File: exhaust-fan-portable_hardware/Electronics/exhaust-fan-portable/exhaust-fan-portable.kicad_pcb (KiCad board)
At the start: 2 copper layers, 68 parts, among them J1 Conn_01x04_Pin, J2 Conn_01x04_Pin, J3 Conn_01x04_Pin, J4 Conn_01x04_Pin, J6 Barrel_Jack_MountingPin, J7 Conn_01x04_Pin, J9 Conn_01x06_Socket, P1 USB_C_Plug_USB2.0, Q1 NMOS, Q2 NMOS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

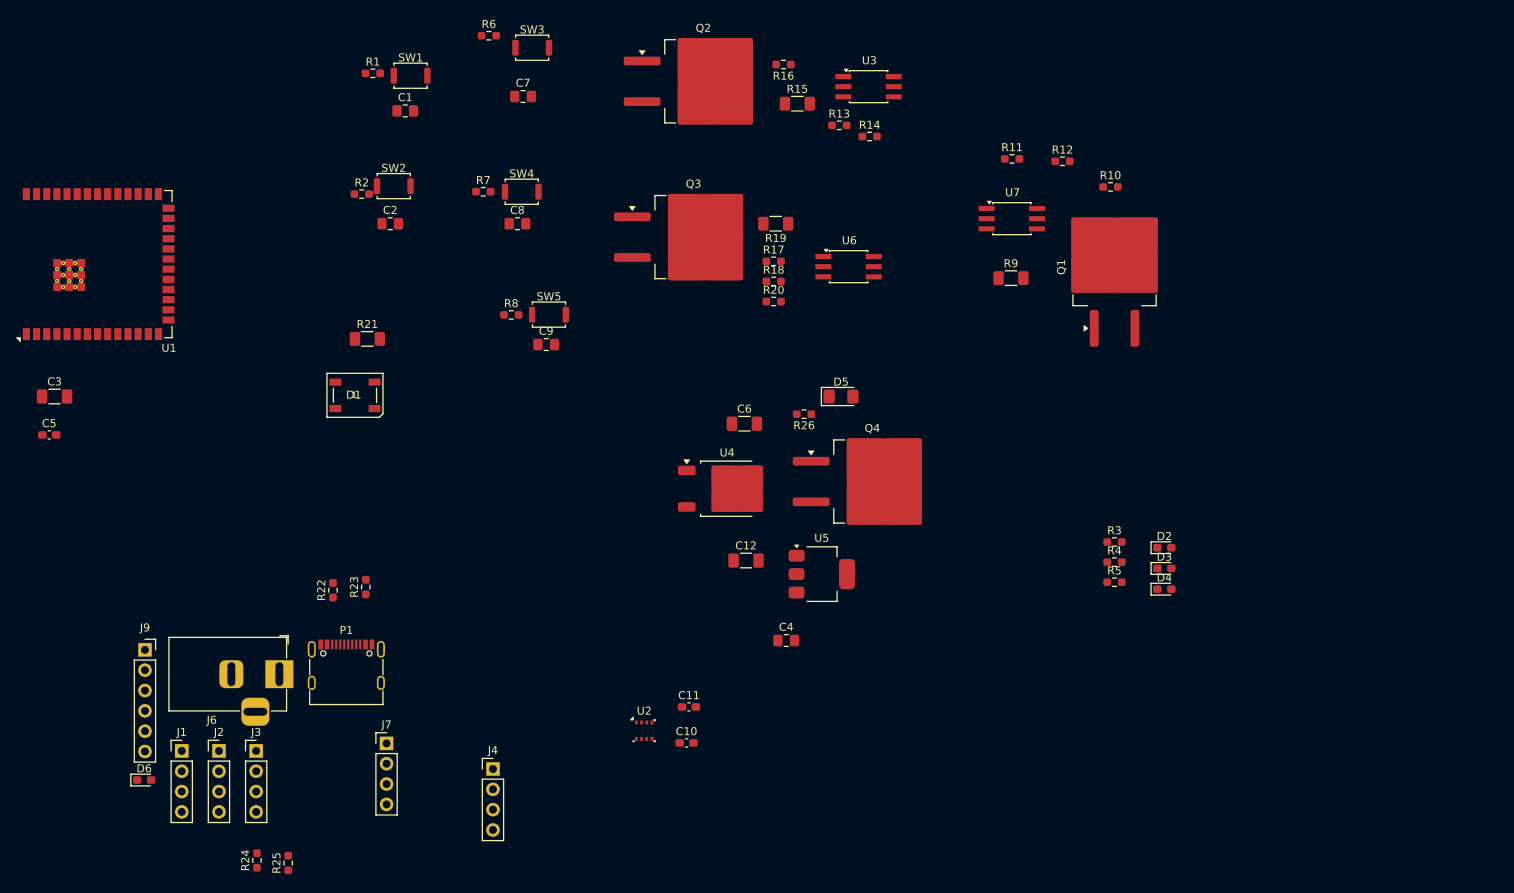
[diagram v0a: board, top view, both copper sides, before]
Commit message: updated mechanical information
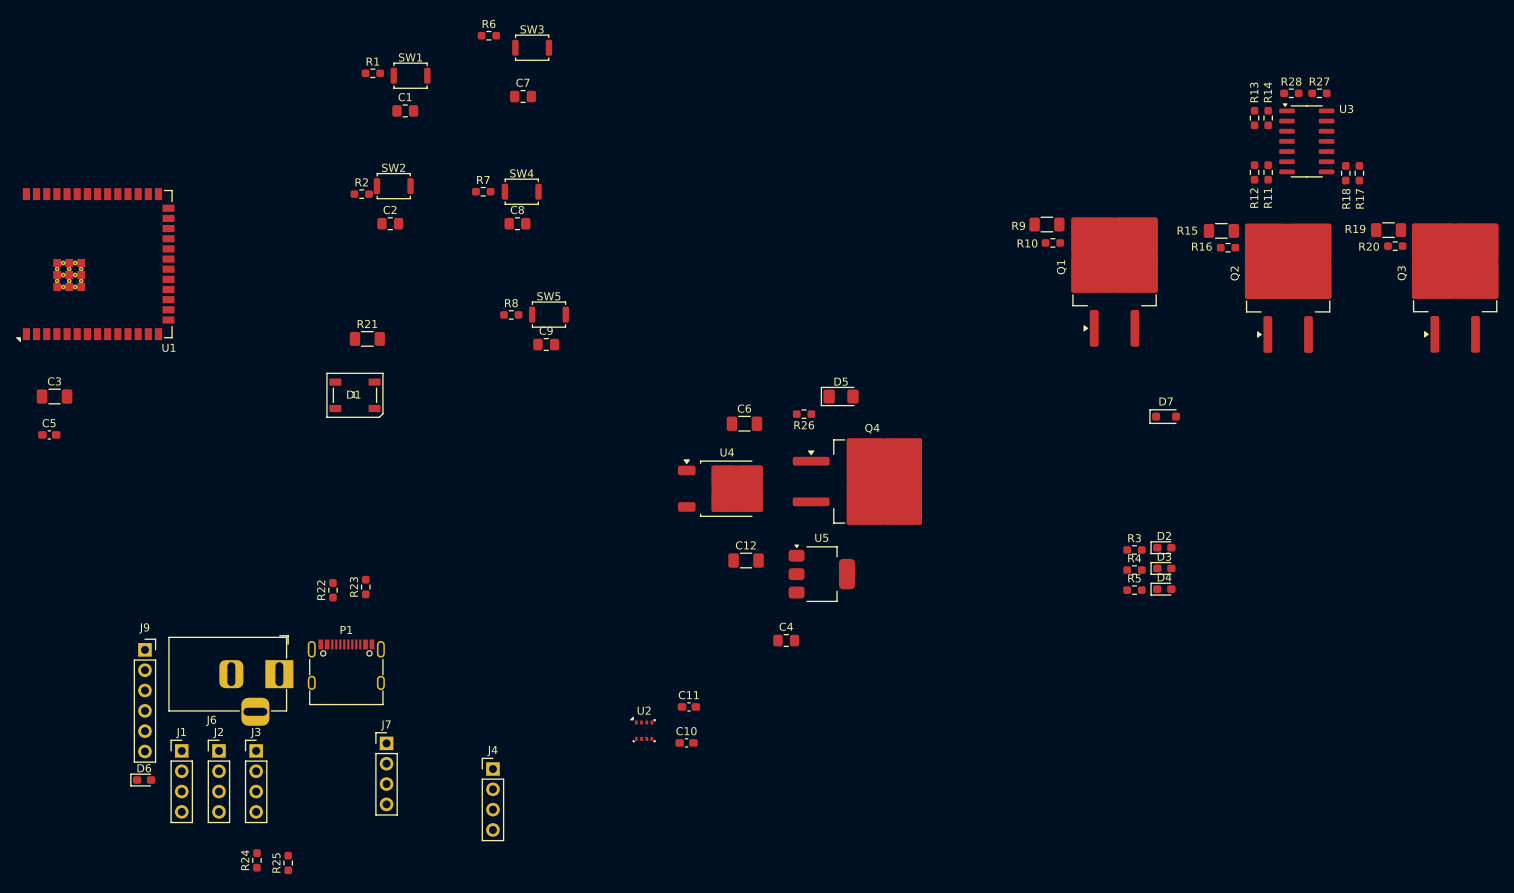
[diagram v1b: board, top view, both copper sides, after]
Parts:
- removed U6, U7: LMV321, Package_SO:SO-6_4.4x3.6mm_P1.27mm
- added D7: 1N4001, Diode_SMD:D_SOD-323_HandSoldering, F.Cu at (228.1, 93.1)
- added R27: 50K, Resistor_SMD:R_0603_1608Metric_Pad0.98x0.95mm_HandSolder, F.Cu at (247.3, 52.7)
- added R28: 50K, Resistor_SMD:R_0603_1608Metric_Pad0.98x0.95mm_HandSolder, F.Cu at (243.8, 52.7)
- D5: value D_Zener -> >11.3
- Q1, Q2, Q3, Q4: value NMOS -> HY1906P
- R15, R19, R9: value 470 -> 600
- R3: value 10K -> 5K
- R4: value 10K -> 2K
- R5: value 10K -> 1K
- U3: value LMV321 -> TL074; footprint Package_SO:SO-6_4.4x3.6mm_P1.27mm -> Package_SO:SOIC-14_3.9x8.7mm_P1.27mm
- moved Q3 95.3 mm to (264.3, 75.2), turned to 90 degrees
- moved R20 78.0 mm to (256.8, 71.8)
- moved Q2 76.9 mm to (243.4, 75.2), turned to 90 degrees
- moved R19 76.6 mm to (255.9, 69.8)
- moved R17 74.0 mm to (252.3, 62.7), turned to -90 degrees
- moved R18 72.8 mm to (250.6, 62.7), turned to -90 degrees
- moved R16 60.1 mm to (235.9, 72.0)
- moved R15 55.3 mm to (235.1, 69.9)
- moved U3 55.2 mm to (245.7, 58.7)
- moved R13 51.9 mm to (239.2, 55.8), turned to -90 degrees
- moved R14 49.9 mm to (240.9, 55.8), turned to 90 degrees
- moved R11 32.1 mm to (240.9, 62.6), turned to -90 degrees
- moved R12 24.1 mm to (239.2, 62.6), turned to -90 degrees
- moved R10 10.0 mm to (214.0, 71.4)
- moved R9 8.07 mm to (213.2, 69.1)
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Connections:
- D5 pad 2: GND -> Net-(D5-A)
- R11 pad 1: Net-(U7--) -> Net-(U3B--)
- R12 pad 1: GND -> Net-(U3B--)
- R12 pad 2: Net-(U7--) -> OPAMP_VREF
- R13 pad 1: GND -> OPAMP_VREF
- R13 pad 2: Net-(U3--) -> Net-(U3A--)
- R14 pad 1: Net-(U3--) -> Net-(U3A--)
- R17 pad 1: GND -> Net-(U3C--)
- R17 pad 2: Net-(U6--) -> OPAMP_VREF
- R18 pad 1: Net-(U6--) -> Net-(U3C--)
- U3 pad 1: FAN1_CTRL_PWR -> Net-(R14-Pad2)
- U3 pad 2: GND -> Net-(U3A--)
- U3 pad 3: Net-(U3--) -> FAN1_CTRL_PWR
- U3 pad 4: Net-(R14-Pad2) -> +12V
- U3 pad 5: +5V -> FAN2_CTRL_PWR
- U3 pad 6: (no net) -> Net-(U3B--)
